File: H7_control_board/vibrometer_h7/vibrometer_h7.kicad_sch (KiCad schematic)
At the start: 0 parts

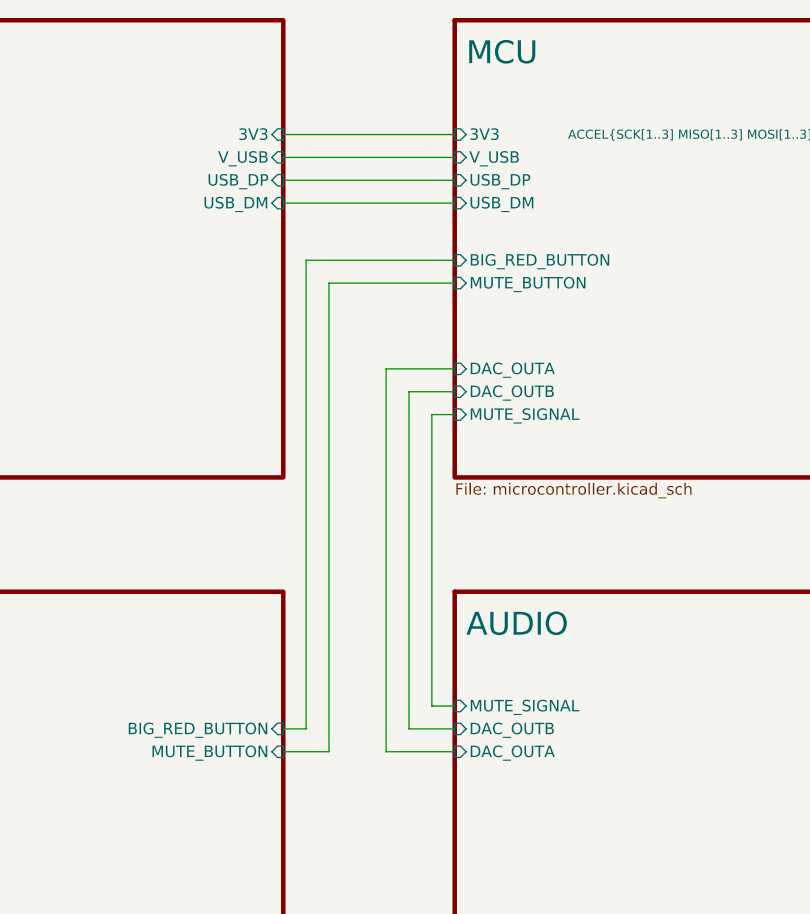
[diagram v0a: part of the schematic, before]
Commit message: cleaned up silkscreen
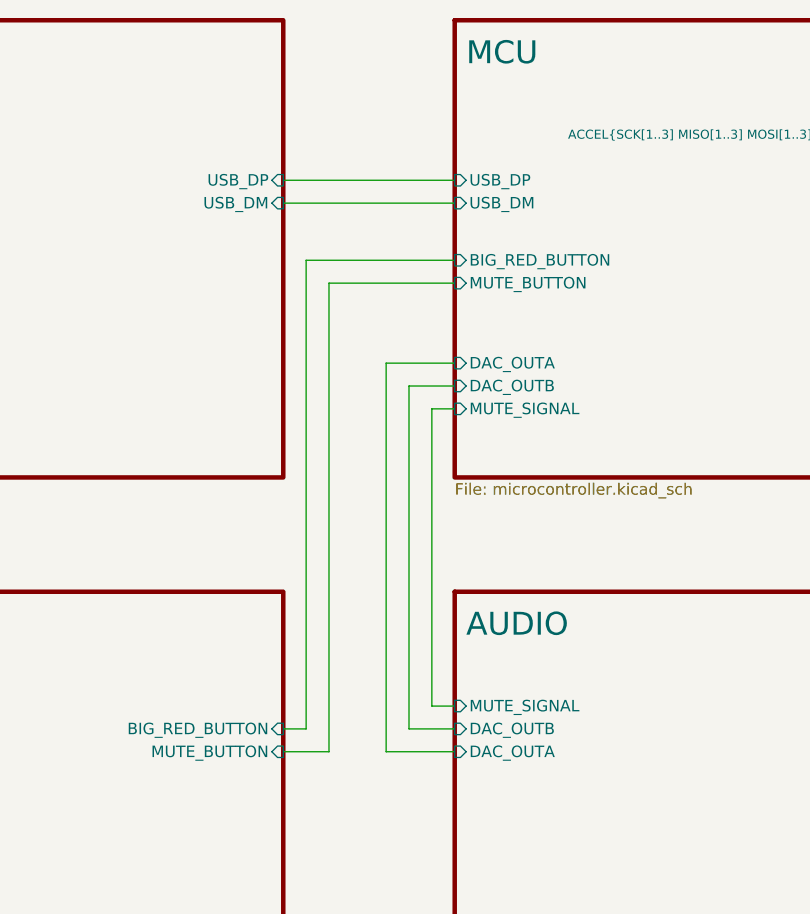
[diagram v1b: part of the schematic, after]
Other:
- sheet MCU ports: added none; removed 3V3, V_USB
- sheet USB ports: added none; removed 3V3, V_USB
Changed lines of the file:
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@@
 	(wire
 		(pts
-			(xy 95.25 53.34) (xy 114.3 53.34)
-		)
-		(stroke
-			(width 0)
-			(type default)
-		)
-	)
-	(wire
-		(pts
-			(xy 109.22 79.375) (xy 109.22 116.84)
-		)
-		(stroke
-			(width 0)
-			(type default)
-		)
-	)
-	(wire
-		(pts
-			(xy 114.3 76.835) (xy 106.68 76.835)
+			(xy 109.22 78.74) (xy 109.22 116.84)
+		)
+		(stroke
+			(width 0)
+			(type default)
+		)
+	)
+	(wire
+		(pts
+			(xy 114.3 76.2) (xy 106.68 76.2)
 		)
 		(stroke
@@
 	(wire
 		(pts
-			(xy 106.68 76.835) (xy 106.68 119.38)
+			(xy 106.68 76.2) (xy 106.68 119.38)
 		)
 		(stroke
@@
 	(wire
 		(pts
-			(xy 114.3 79.375) (xy 109.22 79.375)
-		)
-		(stroke
-			(width 0)
-			(type default)
-		)
-	)
-	(wire
-		(pts
-			(xy 114.3 81.915) (xy 111.76 81.915)
+			(xy 114.3 78.74) (xy 109.22 78.74)
+		)
+		(stroke
+			(width 0)
+			(type default)
+		)
+	)
+	(wire
+		(pts
+			(xy 114.3 81.28) (xy 111.76 81.28)
 		)
 		(stroke
@@
 	(wire
 		(pts
-			(xy 111.76 81.915) (xy 111.76 114.3)
-		)
-		(stroke
-			(width 0)
-			(type default)
-		)
-	)
-	(wire
-		(pts
-			(xy 95.25 50.8) (xy 114.3 50.8)
+			(xy 111.76 81.28) (xy 111.76 114.3)
 		)
 		(stroke
@@
 			)
 		)
-		(pin "3V3" input
-			(at 114.3 50.8 180)
-			(effects
-				(font
-					(size 1.27 1.27)
-				)
-				(justify left)
-			)
-		)
-		(pin "V_USB" input
-			(at 114.3 53.34 180)
-			(effects
-				(font
-					(size 1.27 1.27)
-				)
-				(justify left)
-			)
-		)
 		(pin "USB_DM" input
 			(at 114.3 58.42 180)
@@
 		)
 		(pin "DAC_OUTA" input
-			(at 114.3 76.835 180)
+			(at 114.3 76.2 180)
 			(effects
 				(font
@@
 		)
 		(pin "DAC_OUTB" input
-			(at 114.3 79.375 180)
+			(at 114.3 78.74 180)
 			(effects
 				(font
@@
 		)
 		(pin "MUTE_SIGNAL" input
-			(at 114.3 81.915 180)
+			(at 114.3 81.28 180)
 			(effects
 				(font
@@
 			)
 		)
-		(pin "3V3" input
-			(at 95.25 50.8 0)
-			(effects
-				(font
-					(size 1.27 1.27)
-				)
-				(justify right)
-			)
-		)
-		(pin "V_USB" input
-			(at 95.25 53.34 0)
-			(effects
-				(font
-					(size 1.27 1.27)
-				)
-				(justify right)
-			)
-		)

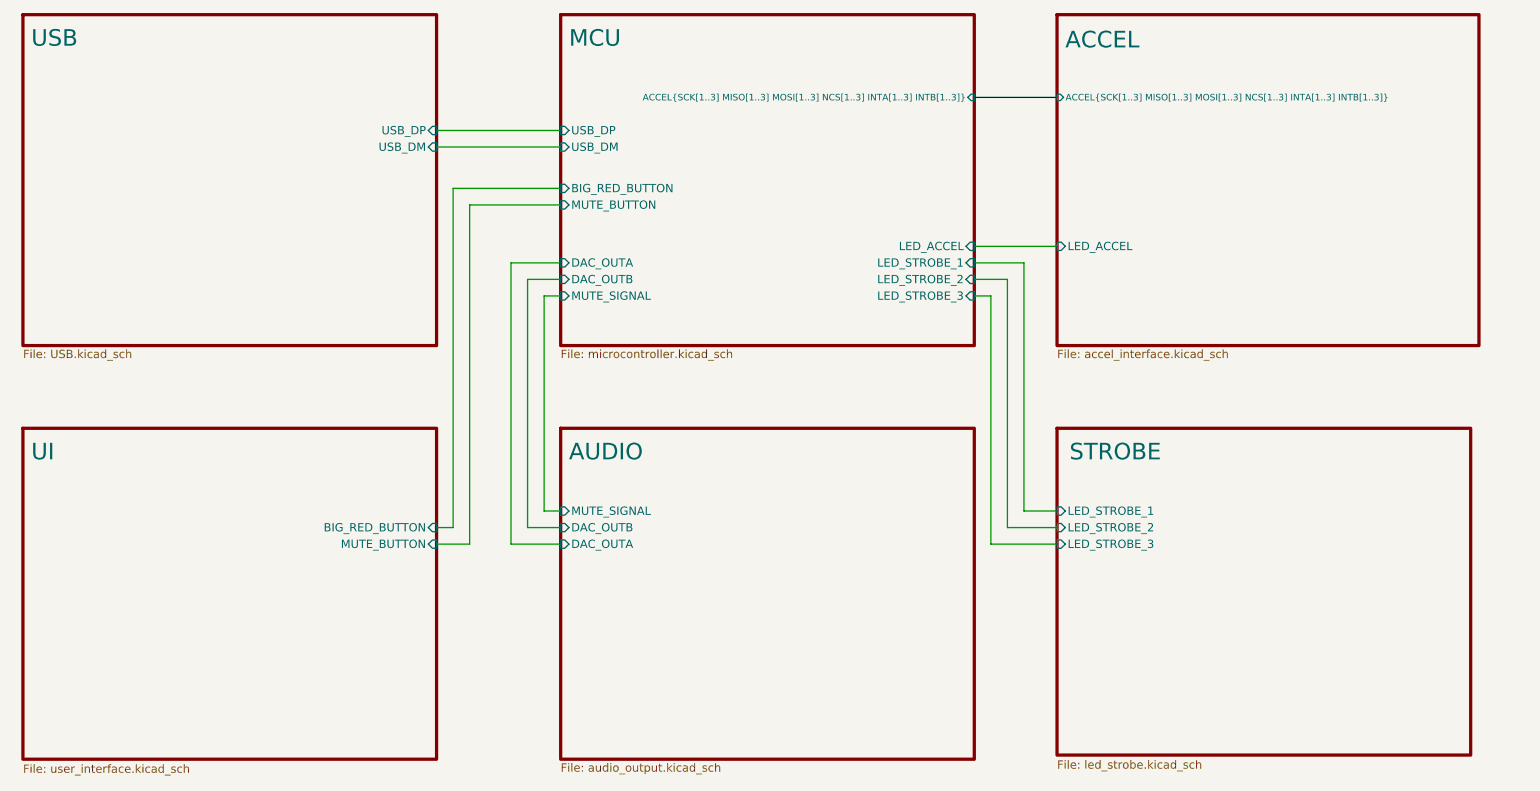
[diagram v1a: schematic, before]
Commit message: added indicator leds
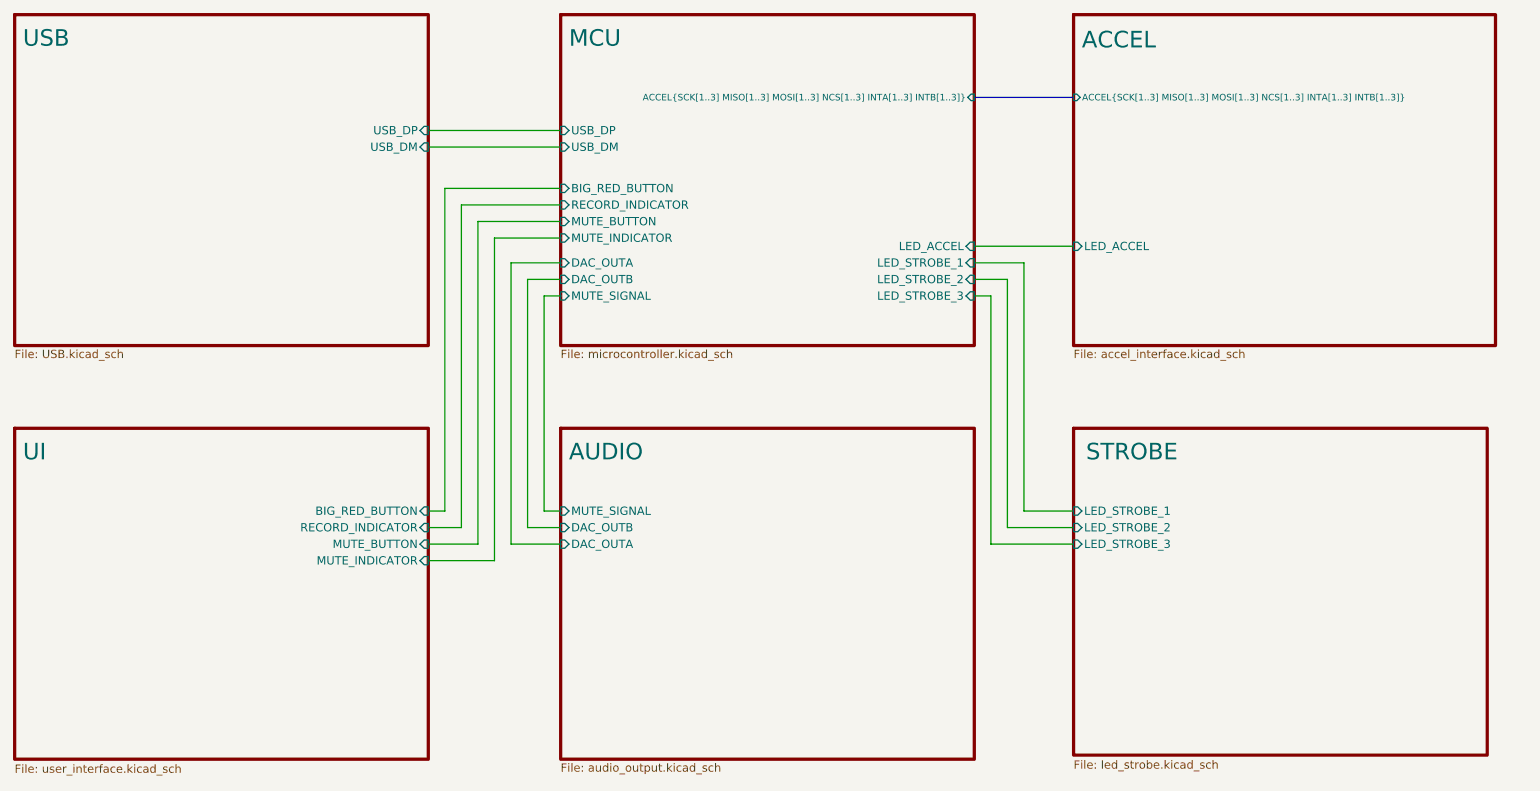
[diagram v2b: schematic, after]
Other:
- sheet MCU ports: added MUTE_INDICATOR, RECORD_INDICATOR; removed none
- sheet UI ports: added MUTE_INDICATOR, RECORD_INDICATOR; removed none
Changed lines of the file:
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@@
 	(wire
 		(pts
-			(xy 185.42 114.3) (xy 190.5 114.3)
+			(xy 185.42 114.3) (xy 193.04 114.3)
+		)
+		(stroke
+			(width 0)
+			(type default)
+		)
+	)
+	(wire
+		(pts
+			(xy 93.98 121.92) (xy 104.14 121.92)
+		)
+		(stroke
+			(width 0)
+			(type default)
+		)
+	)
+	(wire
+		(pts
+			(xy 93.98 116.84) (xy 99.06 116.84)
 		)
 		(stroke
@@
 	(wire
 		(pts
-			(xy 95.25 58.42) (xy 114.3 58.42)
+			(xy 93.98 58.42) (xy 114.3 58.42)
+		)
+		(stroke
+			(width 0)
+			(type default)
+		)
+	)
+	(wire
+		(pts
+			(xy 99.06 67.31) (xy 114.3 67.31)
 		)
 		(stroke
@@
 	(wire
 		(pts
+			(xy 104.14 72.39) (xy 114.3 72.39)
+		)
+		(stroke
+			(width 0)
+			(type default)
+		)
+	)
+	(wire
+		(pts
 			(xy 114.3 76.2) (xy 106.68 76.2)
 		)
@@
 	(wire
 		(pts
-			(xy 177.8 73.66) (xy 190.5 73.66)
-		)
-		(stroke
-			(width 0)
-			(type default)
-		)
-	)
-	(wire
-		(pts
-			(xy 97.79 64.77) (xy 97.79 116.84)
+			(xy 177.8 73.66) (xy 193.04 73.66)
+		)
+		(stroke
+			(width 0)
+			(type default)
+		)
+	)
+	(wire
+		(pts
+			(xy 96.52 64.77) (xy 96.52 114.3)
 		)
 		(stroke
@@
 	(wire
 		(pts
-			(xy 100.33 67.31) (xy 114.3 67.31)
-		)
-		(stroke
-			(width 0)
-			(type default)
-		)
-	)
-	(wire
-		(pts
-			(xy 100.33 119.38) (xy 95.25 119.38)
-		)
-		(stroke
-			(width 0)
-			(type default)
-		)
-	)
-	(wire
-		(pts
-			(xy 97.79 116.84) (xy 95.25 116.84)
-		)
-		(stroke
-			(width 0)
-			(type default)
-		)
-	)
-	(wire
-		(pts
-			(xy 114.3 64.77) (xy 97.79 64.77)
+			(xy 101.6 69.85) (xy 114.3 69.85)
+		)
+		(stroke
+			(width 0)
+			(type default)
+		)
+	)
+	(wire
+		(pts
+			(xy 101.6 119.38) (xy 93.98 119.38)
+		)
+		(stroke
+			(width 0)
+			(type default)
+		)
+	)
+	(wire
+		(pts
+			(xy 96.52 114.3) (xy 93.98 114.3)
+		)
+		(stroke
+			(width 0)
+			(type default)
+		)
+	)
+	(wire
+		(pts
+			(xy 114.3 64.77) (xy 96.52 64.77)
 		)
 		(stroke
@@
 	(bus
 		(pts
-			(xy 177.8 50.8) (xy 190.5 50.8)
+			(xy 177.8 50.8) (xy 193.04 50.8)
 		)
 		(stroke
@@
 	(wire
 		(pts
+			(xy 104.14 121.92) (xy 104.14 72.39)
+		)
+		(stroke
+			(width 0)
+			(type default)
+		)
+	)
+	(wire
+		(pts
+			(xy 99.06 116.84) (xy 99.06 67.31)
+		)
+		(stroke
+			(width 0)
+			(type default)
+		)
+	)
+	(wire
+		(pts
 			(xy 106.68 76.2) (xy 106.68 119.38)
 		)
@@
 	(wire
 		(pts
-			(xy 182.88 116.84) (xy 190.5 116.84)
-		)
-		(stroke
-			(width 0)
-			(type default)
-		)
-	)
-	(wire
-		(pts
-			(xy 95.25 55.88) (xy 114.3 55.88)
+			(xy 182.88 116.84) (xy 193.04 116.84)
+		)
+		(stroke
+			(width 0)
+			(type default)
+		)
+	)
+	(wire
+		(pts
+			(xy 93.98 55.88) (xy 114.3 55.88)
 		)
 		(stroke
@@
 	(wire
 		(pts
-			(xy 180.34 119.38) (xy 190.5 119.38)
+			(xy 180.34 119.38) (xy 193.04 119.38)
 		)
 		(stroke
@@
 	(wire
 		(pts
-			(xy 100.33 67.31) (xy 100.33 119.38)
+			(xy 101.6 69.85) (xy 101.6 119.38)
 		)
 		(stroke
@@
 		)
 		(pin "MUTE_BUTTON" input
-			(at 114.3 67.31 180)
+			(at 114.3 69.85 180)
 			(effects
 				(font
@@
 				)
 				(justify right)
+			)
+		)
+		(pin "MUTE_INDICATOR" input
+			(at 114.3 72.39 180)
+			(effects
+				(font
+					(size 1.27 1.27)
+				)
+				(justify left)
+			)
+		)
+		(pin "RECORD_INDICATOR" input
+			(at 114.3 67.31 180)
+			(effects
+				(font
+					(size 1.27 1.27)
+				)
+				(justify left)
 			)
 		)
@@
 	)
 	(sheet
-		(at 31.75 101.6)
+		(at 30.48 101.6)
 		(size 63.5 50.8)
 		(stroke
@@
 		)
 		(property "Sheetname" "UI"
-			(at 33.02 106.68 0)
+			(at 31.75 106.68 0)
 			(effects
 				(font
@@
 		)
 		(property "Sheetfile" "user_interface.kicad_sch"
-			(at 31.75 153.1584 0)
+			(at 30.48 153.1584 0)
 			(effects
 				(font
@@
 		)
 		(pin "BIG_RED_BUTTON" input
-			(at 95.25 116.84 0)
+			(at 93.98 114.3 0)
 			(effects
 				(font
@@
 		)
 		(pin "MUTE_BUTTON" input
-			(at 95.25 119.38 0)
+			(at 93.98 119.38 0)
+			(effects
+				(font
+					(size 1.27 1.27)
+				)
+				(justify right)
+			)
+		)
+		(pin "MUTE_INDICATOR" input
+			(at 93.98 121.92 0)
+			(effects
+				(font
+					(size 1.27 1.27)
+				)
+				(justify right)
+			)
+		)
+		(pin "RECORD_INDICATOR" input
+			(at 93.98 116.84 0)
 			(effects
 				(font
@@
 	)
 	(sheet
-		(at 31.75 38.1)
+		(at 30.48 38.1)
 		(size 63.5 50.8)
 		(stroke
@@
 		)
 		(property "Sheetname" "USB"
-			(at 33.02 43.18 0)
+			(at 31.75 43.18 0)
 			(effects
 				(font
@@
 		)
 		(property "Sheetfile" "USB.kicad_sch"
-			(at 31.75 89.4846 0)
+			(at 30.48 89.4846 0)
 			(effects
 				(font
@@
 		)
 		(pin "USB_DM" input
-			(at 95.25 58.42 0)
+			(at 93.98 58.42 0)
 			(effects
 				(font
@@
 		)
 		(pin "USB_DP" input
-			(at 95.25 55.88 0)
+			(at 93.98 55.88 0)
 			(effects
 				(font
@@
 	)
 	(sheet
-		(at 190.5 101.6)
+		(at 193.04 101.6)
 		(size 63.5 50.165)
 		(stroke
@@
 		)
 		(property "Sheetname" "STROBE"
-			(at 192.405 106.68 0)
+			(at 194.945 106.68 0)
 			(effects
 				(font
@@
 		)
 		(property "Sheetfile" "led_strobe.kicad_sch"
-			(at 190.5 152.5234 0)
+			(at 193.04 152.5234 0)
 			(effects
 				(font
@@
 		)
 		(property "Field2" ""
-			(at 190.5 101.6 0)
+			(at 193.04 101.6 0)
 			(effects
 				(font
@@
 		)
 		(pin "LED_STROBE_3" input
-			(at 190.5 119.38 180)
+			(at 193.04 119.38 180)
 			(effects
 				(font
@@
 		)
 		(pin "LED_STROBE_1" input
-			(at 190.5 114.3 180)
+			(at 193.04 114.3 180)
 			(effects
 				(font
@@
 		)
 		(pin "LED_STROBE_2" input
-			(at 190.5 116.84 180)
+			(at 193.04 116.84 180)
 			(effects
 				(font
@@
 	)
 	(sheet
-		(at 190.5 38.1)
+		(at 193.04 38.1)
 		(size 64.77 50.8)
 		(stroke
@@
 		)
 		(property "Sheetname" "ACCEL"
-			(at 191.77 43.434 0)
+			(at 194.31 43.434 0)
 			(effects
 				(font
@@
 		)
 		(property "Sheetfile" "accel_interface.kicad_sch"
-			(at 190.5 89.4846 0)
+			(at 193.04 89.4846 0)
 			(effects
 				(font
@@
 		(pin "ACCEL{SCK[1..3] MISO[1..3] MOSI[1..3] NCS[1..3] INTA[1..3] INTB[1..3]}"
 			input
-			(at 190.5 50.8 180
+			(at 193.04 50.8 180
 			)
 			(effects
@@
 		)
 		(pin "LED_ACCEL" input
-			(at 190.5 73.66 180)
-			(effects
-				(font
+			(at 193.04 73.66 180)
+			(effects
+				(font
